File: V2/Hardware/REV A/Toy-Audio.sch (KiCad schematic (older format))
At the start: 24 parts, among them J1 CONN_01X02, J2 CONN_01X04, J3 CONN_01X03, J4 CONN_01X03, J5 CONN_01X04, U1 XC6206P332MR, U2 STM32F030F4P6, U3 W25Q32FVSIG, U4 TS4890

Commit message: Changed Toy-Audio.sch HW V2 REV A low Pass filter (removed voltage divider) to increase the speaker sound volume
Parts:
- R3: value 1k8 -> 910R
- R5: value 1k8 -> D.N.P
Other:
- note added: "D.N.P = Do Not Populate"
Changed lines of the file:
@@
 P 5750 4350
 F 0 "R5" V 5830 4350 50  0000 C CNN
-F 1 "1k8" V 5675 4350 50  0000 C CNN
+F 1 "D.N.P" V 5675 4350 50  0000 C CNN
 F 2 "MvdL:R0603" H 5750 4350 60  0001 C CNN
 F 3 "" H 5750 4350 60  0000 C CNN
@@
 P 5450 4100
 F 0 "R3" V 5530 4100 50  0000 C CNN
-F 1 "1k8" V 5375 4100 50  0000 C CNN
+F 1 "910R" V 5375 4100 50  0000 C CNN
 F 2 "MvdL:R0603" H 5450 4100 60  0001 C CNN
 F 3 "" H 5450 4100 60  0000 C CNN
@@
 Wire Wire Line
 	2550 1700 2550 1800
+Text Notes 6050 4700 0    60   ~ 0
+D.N.P = Do Not Populate
 $EndSCHEMATC

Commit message: Modified PCB layout, improved hand solderability.
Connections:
- net SP+: now reaches R7.1, SP1.1 (P1), U4.5 (Vout1)
- net SP-: now reaches SP1.2 (P2), U4.8 (Vout2)
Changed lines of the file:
@@
 Title "Toy audio"
 Date "5 aug 2015"
-Rev "C"
+Rev "A"
 Comp ""
 Comment1 ""
@@
 Text Notes 6050 4700 0    60   ~ 0
 D.N.P = Do Not Populate
+Text Label 8800 4200 0    60   ~ 0
+SP+
+Text Label 8800 4400 0    60   ~ 0
+SP-
 $EndSCHEMATC

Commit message: Added Standby mode to software V1. Modified hardware to support Standby (add pull up/down resistors) todo hardware V3
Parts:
- added R8: 100k, MvdL:R0603, symbol RR
- U4: footprint myfootprints VDL:SSOP-8 -> MvdL:MSOP8
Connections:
- net GND: now also R8.1
- net nMUTE: now also R8.2

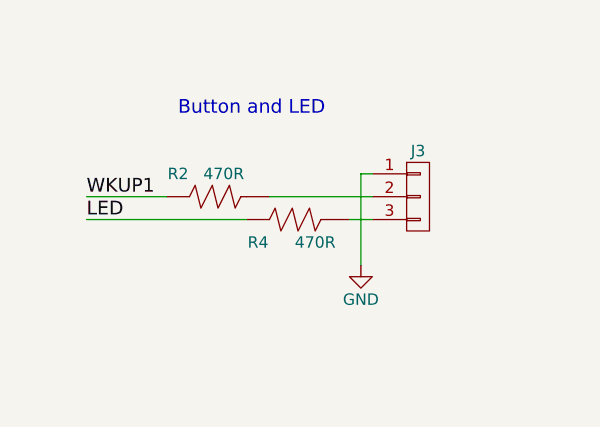
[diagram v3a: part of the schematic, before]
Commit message: Improved Wake-up pin stability WKUP1. modiefied schematic files. Software V1 is compatible with hardware V2
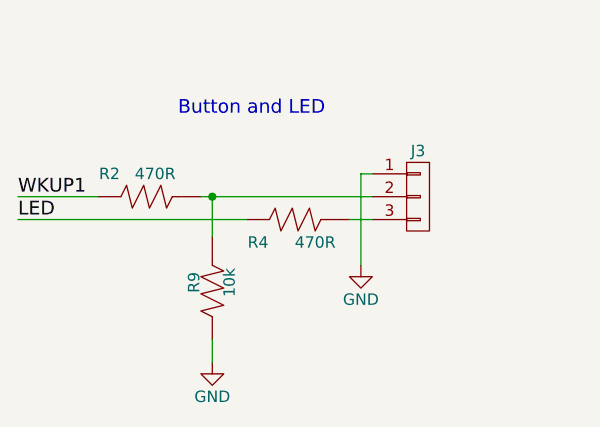
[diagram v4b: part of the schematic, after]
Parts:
- added R9: 10k, MvdL:R0603, symbol RR
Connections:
- net GND: now also R9.1
- net at J3.2 (P2), R2.2: now also R9.2
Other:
- moved on the sheet: R2
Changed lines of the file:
@@
 L RR R2
 U 1 1 566EF481
-P 1600 5900
-F 0 "R2" V 1700 6100 50  0000 C CNN
-F 1 "470R" V 1700 5900 50  0000 C CNN
-F 2 "MvdL:R0603" H 1600 5900 60  0001 C CNN
-F 3 "" H 1600 5900 60  0000 C CNN
-	1    1600 5900
+P 1300 5900
+F 0 "R2" V 1400 6100 50  0000 C CNN
+F 1 "470R" V 1400 5900 50  0000 C CNN
+F 2 "MvdL:R0603" H 1300 5900 60  0001 C CNN
+F 3 "" H 1300 5900 60  0000 C CNN
+	1    1300 5900
 	0    -1   -1   0
 $EndComp
-Text Label 1000 5900 0    60   ~ 0
+Text Label 700  5900 0    60   ~ 0
 WKUP1
-Text Label 1000 6000 0    60   ~ 0
+Text Label 700  6000 0    60   ~ 0
 LED
 $Comp
@@
 	2200 5800 2200 6200
 Wire Wire Line
-	1800 5900 2250 5900
+	1500 5900 2250 5900
 Wire Wire Line
 	2150 6000 2250 6000
 Wire Wire Line
-	1000 5900 1350 5900
-Wire Wire Line
-	1000 6000 1700 6000
+	700  5900 1050 5900
+Wire Wire Line
+	700  6000 1700 6000
 Wire Wire Line
 	1500 2250 1500 2000
@@
 Wire Wire Line
 	7275 4850 7275 4900
+$Comp
+L RR R9
+U 1 1 56784EB9
+P 1550 6275
+F 0 "R9" V 1630 6275 50  0000 C CNN
+F 1 "10k" V 1475 6275 50  0000 C CNN
+F 2 "MvdL:R0603" H 1550 6275 60  0001 C CNN
+F 3 "" H 1550 6275 60  0000 C CNN
+	1    1550 6275
+	-1   0    0    1
+$EndComp
+$Comp
+L GND #PWR029
+U 1 1 567850B0
+P 1550 6625
+F 0 "#PWR029" H 1550 6375 50  0001 C CNN
+F 1 "GND" H 1550 6475 50  0000 C CNN
+F 2 "" H 1550 6625 60  0000 C CNN
+F 3 "" H 1550 6625 60  0000 C CNN
+	1    1550 6625
+	1    0    0    -1
+$EndComp
+Wire Wire Line
+	1550 6525 1550 6625
+Wire Wire Line
+	1550 6075 1550 5900
+Connection ~ 1550 5900
 $EndSCHEMATC
